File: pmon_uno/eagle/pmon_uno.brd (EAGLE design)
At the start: 50 x 50 mm, 42 parts, among them J1 USB, J2 USB, Q1 16Mhz, U1 LTC2943, U2 FT232RL, U3 LT1764AEQ, U4 ATMEGA328TQFP32

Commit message: Started to cleanup the pmon uno BOM.
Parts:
- J3: value (none) -> PINHD-1X3
- J4: value (none) -> PINHD-2X3
- R4: device pmon_uno:SHUNT -> pmon_uno:KELVIN-6432
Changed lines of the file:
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@@
 <attribute name="NAME" x="12.954" y="26.8605" size="0.762" layer="25" font="vector" ratio="10" rot="R90"/>
 </element>
-<element name="J4" library="pmon_uno" package="2X03" value="" x="5.969" y="26.924" smashed="yes" rot="R90">
+<element name="J4" library="pmon_uno" package="2X03" value="PINHD-2X3" x="5.969" y="26.924" smashed="yes" rot="R90">
 <attribute name="NAME" x="8.8265" y="30.0355" size="0.762" layer="25" font="vector" ratio="10" rot="SR270"/>
 <attribute name="VALUE" x="10.414" y="23.114" size="1.27" layer="27" rot="R90"/>
@@
 <attribute name="NAME" x="30.607" y="17.2085" size="0.762" layer="25" font="vector" ratio="10"/>
 </element>
-<element name="R4" library="pmon_uno" package="SHUNT" value="0.025R 1%" x="40.64" y="13.335" smashed="yes" rot="R90">
+<element name="R4" library="pmon_uno" package="KELVIN-6432" value="0.025R 1%" x="40.64" y="13.335" smashed="yes" rot="R90">
 <attribute name="NAME" x="35.7867" y="16.2431" size="0.762" layer="25" font="vector" ratio="10"/>
 </element>
@@
 <attribute name="NAME" x="6.604" y="40.64" size="0.762" layer="25" font="vector" ratio="10" rot="R180"/>
 </element>
-<element name="J3" library="pmon_uno" package="1X03" value="" x="36.576" y="5.461" smashed="yes">
+<element name="J3" library="pmon_uno" package="1X03" value="PINHD-1X3" x="36.576" y="5.461" smashed="yes">
 <attribute name="NAME" x="32.6898" y="7.2898" size="0.762" layer="25" font="vector" ratio="10"/>
 <attribute name="VALUE" x="32.766" y="2.286" size="1.27" layer="27"/>

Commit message: Minor Eagle tweaks: 1. Added a debug pin to the logic analyzer signals. 2. Changed the top and bottom drill sizes from 2.5mm to 3mm.
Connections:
- new net DEBUG: U4.2
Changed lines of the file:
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@@
 <signal name="N$6">
 </signal>
-<signal name="N$5">
+<signal name="DEBUG">
+<contactref element="U4" pad="2"/>
 </signal>
 </signals>

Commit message: Minor text tweaks. No semantic change.
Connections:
- net ACTION renamed START
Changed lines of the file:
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@@
 <wire x1="14.224" y1="14.605" x2="14.19225" y2="14.63675" width="0.2032" layer="1"/>
 </signal>
-<signal name="ACTION">
+<signal name="START">
 <contactref element="U4" pad="32"/>
 <wire x1="19.304" y1="23.876" x2="19.425" y2="23.9776" width="0.254" layer="1"/>

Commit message: Updated schematic and board for rev c.
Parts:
- added J5: PINHD-1X3, pmon_uno:1X03
- moved D4 41.3 mm to (24.1, 4.45), turned to 270 degrees
- moved R12 33.7 mm to (24.1, 8.38), turned to 180 degrees
- moved D5 5.08 mm to (29.2, 4.45)
- moved R13 4.95 mm to (29.1, 8.38)
- moved C8 2.89 mm to (22.4, 36.4)
- moved C4 1.33 mm to (35.3, 39.4)
- moved C1 0.64 mm to (35.6, 41.9)
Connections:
- new net N$5: J1.1, J5.3
- net +5V: now also J5.1
- net N$9: now also J5.2; no longer J1.1
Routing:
- net N$5: track 0.00 -> 8.09 mm
- net N$9: track 12.5 -> 20.5 mm
- net +5V: track 88.0 -> 94.5 mm
- net V+: track 49.7 -> 44.7 mm
- net GND: track 289.5 -> 291.4 mm, vias 25 -> 24
- net N$16: track 6.36 -> 7.93 mm
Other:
- board text added: "CHARGER"
- board text added: "ERROR"
- board text added: "MODE"
- board text added: "POWER-PLAY UNO - REV C"
- board text added: "POWER-PLAY UNO Rev C, May 2014 Single-Cell Power Monitor. Github OSH"
- board text added: "START"
- board text added: "VOUT 2A"
- board text removed: "2 AMPS MAX"
- board text removed: "ACTION"
- board text removed: "ERRORS"
- board text removed: "GND"
- board text removed: "PMON_UNO Rev B, May 2014 Single-Cell Power Monitor. Github OSH"
- board text removed: "SETTINGS"
- board text removed: "VBUS"

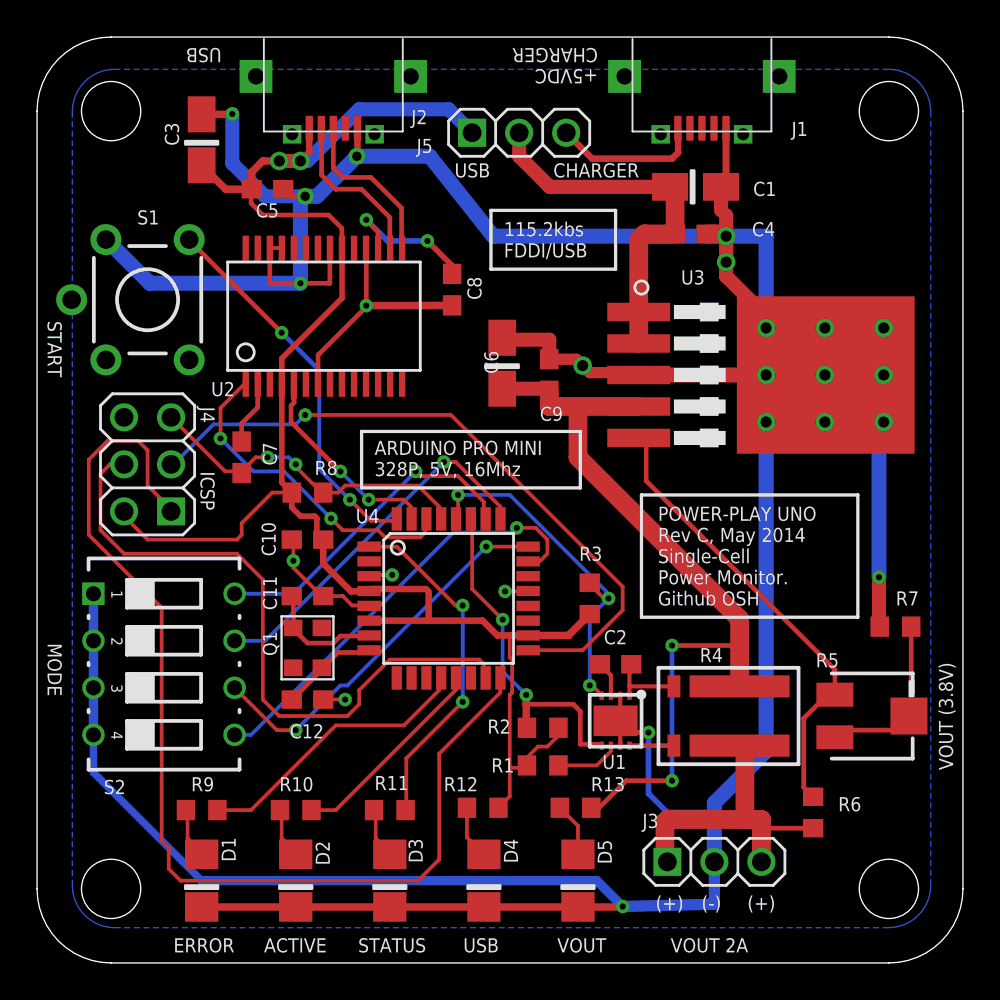
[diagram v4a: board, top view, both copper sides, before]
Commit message: Increased the dril of the USB connector two main support tabs.
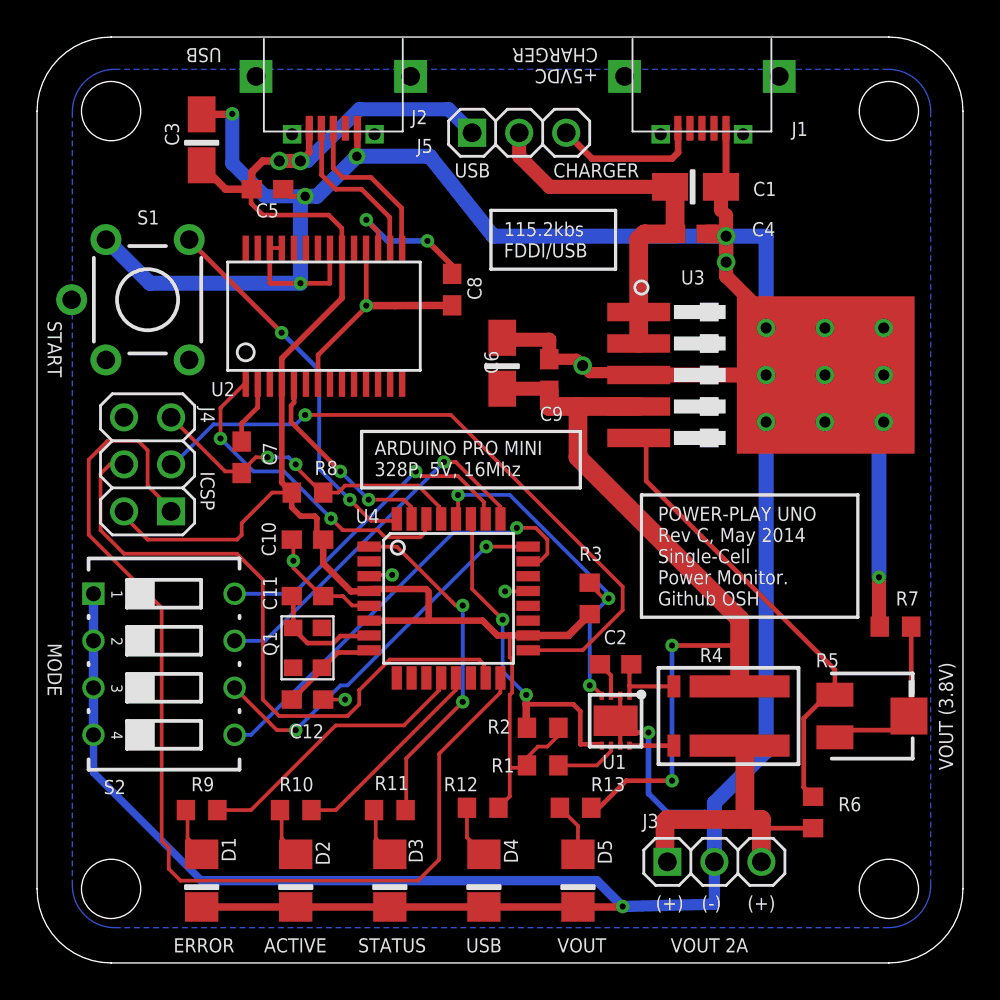
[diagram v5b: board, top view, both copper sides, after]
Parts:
- C7: value 0.1uF -> 0.01uF
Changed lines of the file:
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@@
 <wire x1="31.242" y1="37.465" x2="31.242" y2="40.64" width="0.1778" layer="21"/>
 <wire x1="24.511" y1="37.465" x2="31.242" y2="37.465" width="0.1778" layer="21"/>
-<text x="23.0124" y="0.5715" size="0.762" layer="21" font="vector" ratio="10">USB</text>
+<text x="23.1648" y="0.5715" size="0.762" layer="21" font="vector" ratio="10">USB</text>
 <text x="27.8765" y="42.418" size="0.762" layer="21" font="vector" ratio="10" rot="SR0">CHARGER</text>
 <text x="22.5425" y="42.418" size="0.762" layer="21" font="vector" ratio="10" rot="SR0">USB</text>
@@
 <attribute name="NAME" x="13.081" y="9.271" size="0.762" layer="25" font="vector" ratio="10"/>
 </element>
-<element name="C7" library="pmon_uno" package="C0603" value="0.1uF" x="11.049" y="27.305" smashed="yes" rot="R270">
+<element name="C7" library="pmon_uno" package="C0603" value="0.01uF" x="11.049" y="27.305" smashed="yes" rot="R270">
 <attribute name="NAME" x="12.954" y="26.8605" size="0.762" layer="25" font="vector" ratio="10" rot="R90"/>
 </element>

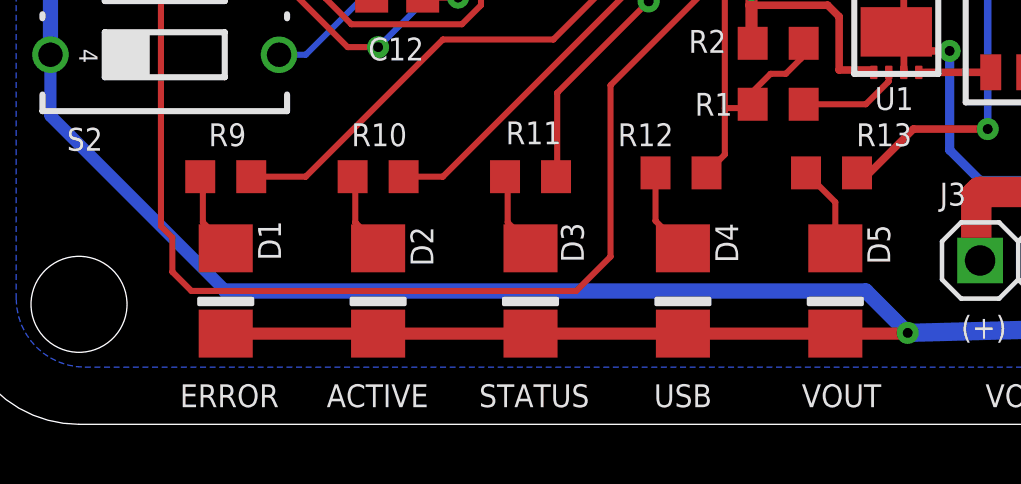
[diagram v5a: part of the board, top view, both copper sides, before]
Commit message: Respaced the LED row.
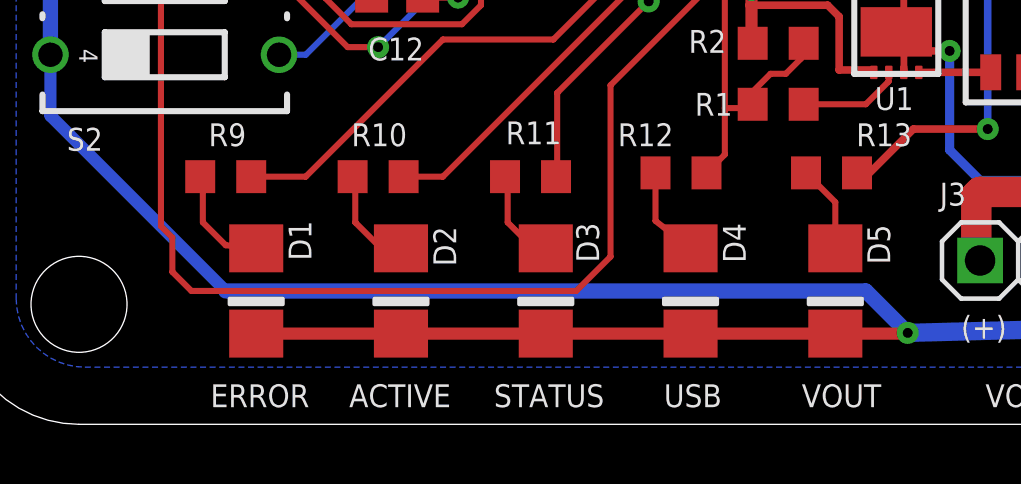
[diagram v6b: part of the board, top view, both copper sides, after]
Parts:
- moved D1 1.02 mm to (9.91, 4.45)
- moved D2 0.76 mm to (14.7, 4.45)
- moved D3 0.51 mm to (19.6, 4.45)
- moved D4 0.25 mm to (24.4, 4.45)
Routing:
- net GND: track 291.4 -> 290.4 mm
- net N$4: track 2.79 -> 3.71 mm
- net N$3: track 2.79 -> 3.46 mm
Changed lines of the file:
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@@
 <board>
 <plain>
-<text x="7.366" y="0.5715" size="0.762" layer="21" font="vector" ratio="10">ERROR</text>
-<text x="12.2555" y="0.5715" size="0.762" layer="21" font="vector" ratio="10">ACTIVE</text>
-<text x="17.3355" y="0.5715" size="0.762" layer="21" font="vector" ratio="10">STATUS</text>
+<text x="8.382" y="0.5715" size="0.762" layer="21" font="vector" ratio="10">ERROR</text>
+<text x="13.0048" y="0.5715" size="0.762" layer="21" font="vector" ratio="10">ACTIVE</text>
+<text x="17.8308" y="0.5715" size="0.762" layer="21" font="vector" ratio="10">STATUS</text>
 <text x="28.0924" y="0.5715" size="0.762" layer="21" font="vector" ratio="10">VOUT</text>
 <text x="33.401" y="2.8575" size="0.762" layer="21" font="vector" ratio="10">(+)</text>
@@
 <wire x1="31.242" y1="37.465" x2="31.242" y2="40.64" width="0.1778" layer="21"/>
 <wire x1="24.511" y1="37.465" x2="31.242" y2="37.465" width="0.1778" layer="21"/>
-<text x="23.1648" y="0.5715" size="0.762" layer="21" font="vector" ratio="10">USB</text>
+<text x="23.495" y="0.5715" size="0.762" layer="21" font="vector" ratio="10">USB</text>
 <text x="27.8765" y="42.418" size="0.762" layer="21" font="vector" ratio="10" rot="SR0">CHARGER</text>
 <text x="22.5425" y="42.418" size="0.762" layer="21" font="vector" ratio="10" rot="SR0">USB</text>
@@
 <attribute name="NAME" x="8.8265" y="30.0355" size="0.762" layer="25" font="vector" ratio="10" rot="SR270"/>
 </element>
-<element name="D1" library="pmon_uno" package="1206-LED" value="RED" x="8.89" y="4.445" smashed="yes" rot="R270">
-<attribute name="NAME" x="10.7315" y="5.461" size="0.762" layer="25" font="vector" ratio="10" rot="R90"/>
-</element>
-<element name="D2" library="pmon_uno" package="1206-LED" value="GREEN" x="13.97" y="4.445" smashed="yes" rot="R270">
-<attribute name="NAME" x="15.8115" y="5.2705" size="0.762" layer="25" font="vector" ratio="10" rot="R90"/>
+<element name="D1" library="pmon_uno" package="1206-LED" value="RED" x="9.906" y="4.445" smashed="yes" rot="R270">
+<attribute name="NAME" x="11.7475" y="5.461" size="0.762" layer="25" font="vector" ratio="10" rot="R90"/>
+</element>
+<element name="D2" library="pmon_uno" package="1206-LED" value="GREEN" x="14.732" y="4.445" smashed="yes" rot="R270">
+<attribute name="NAME" x="16.5735" y="5.2705" size="0.762" layer="25" font="vector" ratio="10" rot="R90"/>
 </element>
 <element name="R8" library="pmon_uno" package="R0603" value="10K" x="14.605" y="25.4" smashed="yes" rot="R180">
@@
 <attribute name="NAME" x="6.9055" y="45.384" size="0.762" layer="25" font="vector" ratio="10" rot="R270"/>
 </element>
-<element name="D4" library="pmon_uno" package="1206-LED" value="BLUE" x="24.13" y="4.445" smashed="yes" rot="R270">
-<attribute name="NAME" x="25.9715" y="5.3848" size="0.762" layer="25" font="vector" ratio="10" rot="R90"/>
+<element name="D4" library="pmon_uno" package="1206-LED" value="BLUE" x="24.384" y="4.445" smashed="yes" rot="R270">
+<attribute name="NAME" x="26.2255" y="5.3848" size="0.762" layer="25" font="vector" ratio="10" rot="R90"/>
 </element>
 <element name="R12" library="pmon_uno" package="R0603" value="3.3K" x="24.0665" y="8.382" smashed="yes" rot="R180">
@@
 <attribute name="NAME" x="25.781" y="11.049" size="0.762" layer="25" font="vector" ratio="10" rot="R180"/>
 </element>
-<element name="D3" library="pmon_uno" package="1206-LED" value="GREEN" x="19.05" y="4.445" smashed="yes" rot="R270">
-<attribute name="NAME" x="20.828" y="5.3975" size="0.762" layer="25" font="vector" ratio="10" rot="R90"/>
+<element name="D3" library="pmon_uno" package="1206-LED" value="GREEN" x="19.558" y="4.445" smashed="yes" rot="R270">
+<attribute name="NAME" x="21.336" y="5.3975" size="0.762" layer="25" font="vector" ratio="10" rot="R90"/>
 </element>
 <element name="R11" library="pmon_uno" package="R0603" value="3.3K" x="19.05" y="8.255" smashed="yes">
@@
 <wire x1="27.6606" y1="32.6" x2="27.6606" y2="33.655" width="0.762" layer="1"/>
 <wire x1="27.6606" y1="33.655" x2="25.6286" y2="33.655" width="0.762" layer="1"/>
-<wire x1="8.89" y1="3.023" x2="13.97" y2="3.023" width="0.4064" layer="1"/>
-<wire x1="13.97" y1="3.023" x2="19.05" y2="3.023" width="0.4064" layer="1"/>
+<wire x1="9.906" y1="3.023" x2="14.732" y2="3.023" width="0.4064" layer="1"/>
+<wire x1="14.732" y1="3.023" x2="19.558" y2="3.023" width="0.4064" layer="1"/>
 <via x="14.478" y="41.402" extent="1-16" drill="0.508"/>
 <wire x1="13.296" y1="41.783" x2="13.677" y2="41.402" width="0.254" layer="1"/>
@@
 <wire x1="6.096" y1="36.703" x2="3.683" y2="39.116" width="0.8128" layer="16"/>
 <wire x1="37.211" y1="39.243" x2="24.638" y2="39.243" width="0.8128" layer="16"/>
-<wire x1="19.05" y1="3.023" x2="24.13" y2="3.023" width="0.4064" layer="1"/>
-<wire x1="29.21" y1="3.023" x2="24.13" y2="3.023" width="0.4064" layer="1"/>
+<wire x1="19.558" y1="3.023" x2="24.384" y2="3.023" width="0.4064" layer="1"/>
+<wire x1="29.21" y1="3.023" x2="24.384" y2="3.023" width="0.4064" layer="1"/>
 <wire x1="31.623" y1="3.048" x2="31.598" y2="3.023" width="0.4064" layer="1"/>
 <wire x1="31.598" y1="3.023" x2="29.21" y2="3.023" width="0.4064" layer="1"/>
@@
 <wire x1="13.97" y1="5.969" x2="13.208" y2="6.731" width="0.2032" layer="1"/>
 <wire x1="13.208" y1="8.255" x2="13.12" y2="8.255" width="0.2032" layer="1"/>
-<wire x1="13.97" y1="5.969" x2="13.97" y2="5.867" width="0.2032" layer="1"/>
+<wire x1="13.97" y1="5.969" x2="14.732" y2="5.867" width="0.2032" layer="1"/>
 </signal>
 <signal name="N$4">
@@
 <wire x1="8.89" y1="5.969" x2="8.128" y2="6.731" width="0.2032" layer="1"/>
 <wire x1="8.128" y1="8.255" x2="8.04" y2="8.255" width="0.2032" layer="1"/>
-<wire x1="8.89" y1="5.969" x2="8.89" y2="5.867" width="0.2032" layer="1"/>
+<wire x1="8.89" y1="5.969" x2="9.906" y2="5.867" width="0.2032" layer="1"/>
 </signal>
 <signal name="+5V">
@@
 <contactref element="R12" pad="2"/>
 <wire x1="23.2165" y1="8.382" x2="23.2165" y2="6.7805" width="0.2032" layer="1"/>
-<wire x1="23.2165" y1="6.7805" x2="24.13" y2="5.867" width="0.2032" layer="1"/>
+<wire x1="23.2165" y1="6.7805" x2="24.384" y2="5.867" width="0.2032" layer="1"/>
 </signal>
 <signal name="SCK">
@@
 <wire x1="19.05" y1="5.969" x2="18.288" y2="6.731" width="0.2032" layer="1"/>
 <wire x1="18.288" y1="8.255" x2="18.2" y2="8.255" width="0.2032" layer="1"/>
-<wire x1="19.05" y1="5.969" x2="19.05" y2="5.867" width="0.2032" layer="1"/>
+<wire x1="19.05" y1="5.969" x2="19.558" y2="5.867" width="0.2032" layer="1"/>
 </signal>
 <signal name="STATUS_LED">
